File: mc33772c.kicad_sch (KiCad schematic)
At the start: 11 parts, among them U2 MC33772CTP1AE

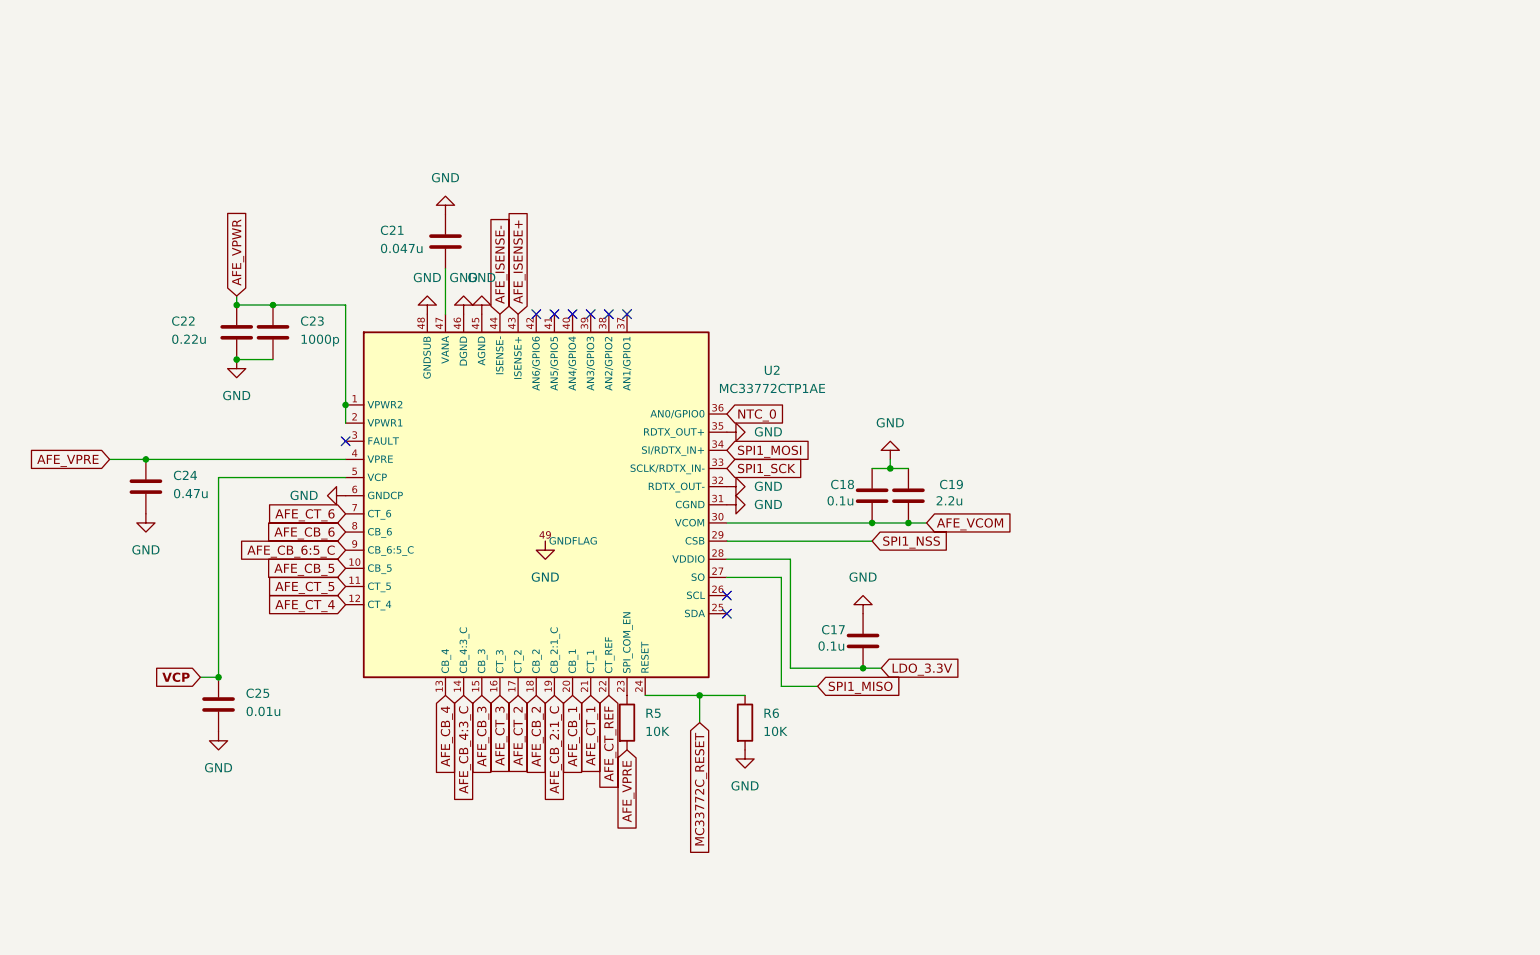
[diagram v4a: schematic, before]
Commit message: add LCPC Part #
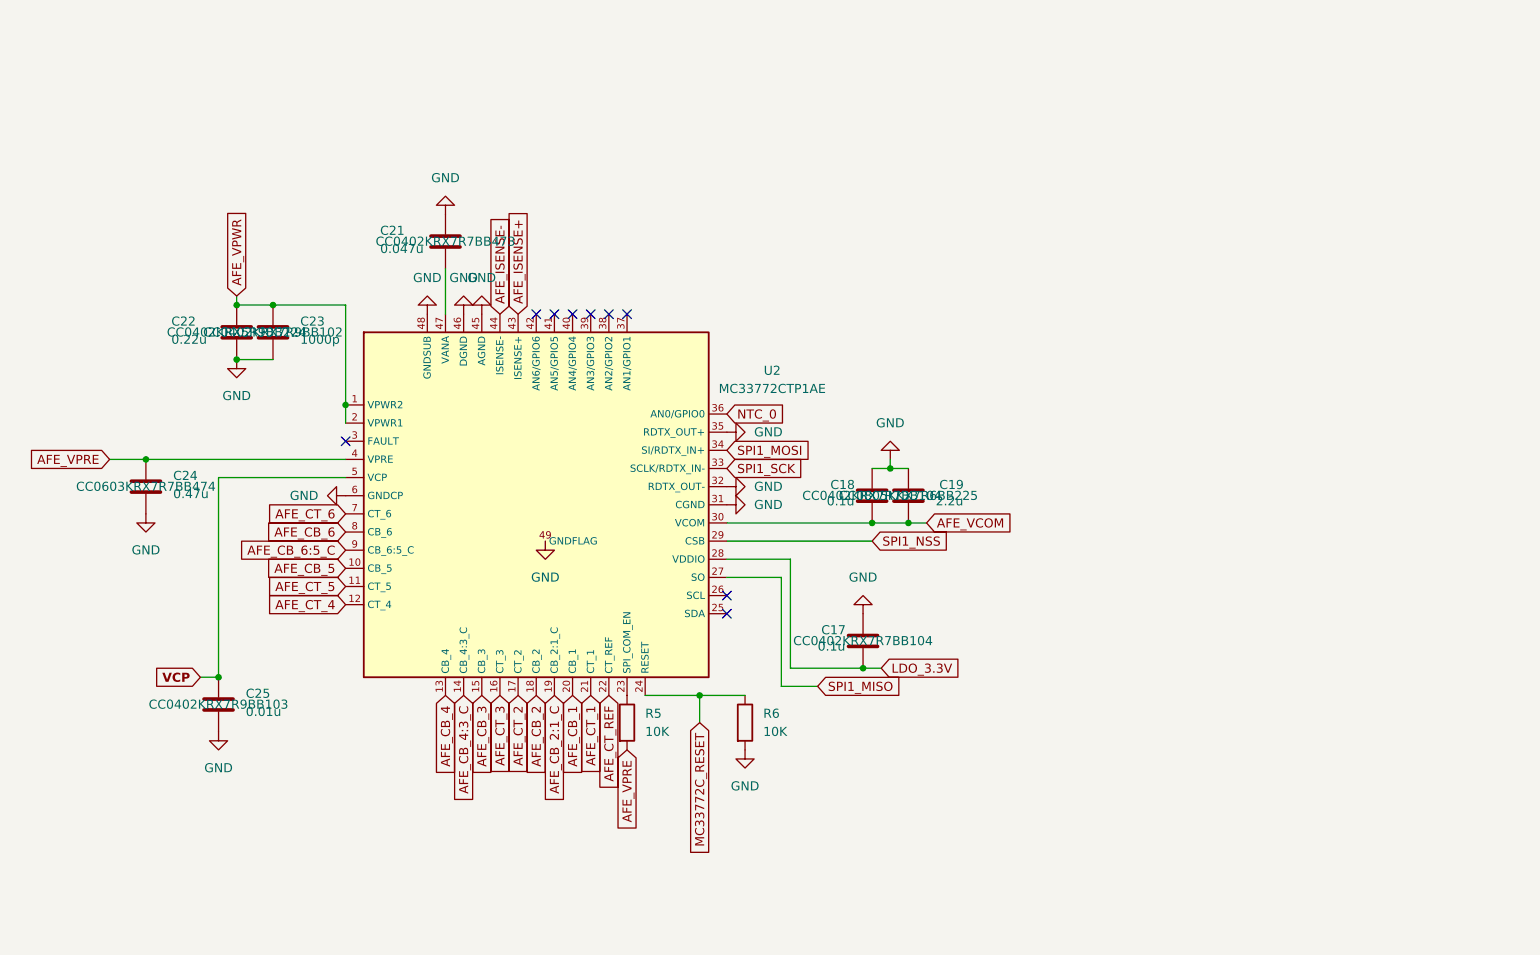
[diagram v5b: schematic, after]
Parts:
- C17, C18: LCSC Part # (none) -> CC0402KRX7R7BB104
- C19: LCSC Part # (none) -> CC0805KKX7R6BB225
- C21: LCSC Part # (none) -> CC0402KRX7R7BB473
- C22: LCSC Part # (none) -> CC0402KRX5R9BB224
- C23: LCSC Part # (none) -> CC0402KRX7R9BB102
- C24: LCSC Part # (none) -> CC0603KRX7R7BB474
- C25: LCSC Part # (none) -> CC0402KRX7R9BB103

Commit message: update for JLCPCB with LCSC part #
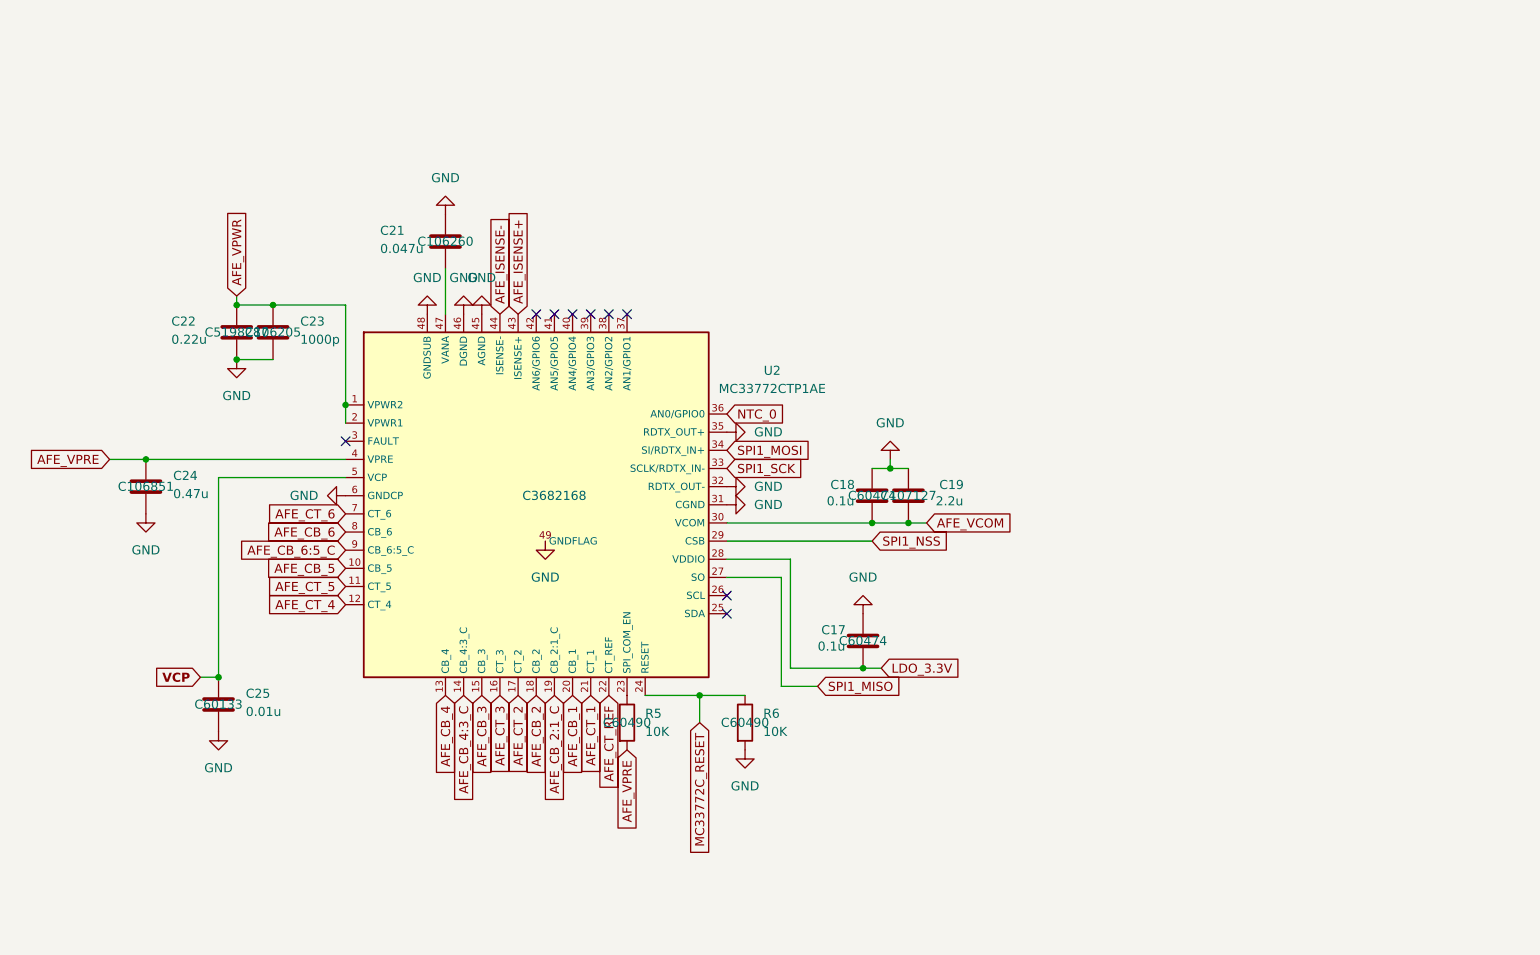
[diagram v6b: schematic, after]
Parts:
- C17, C18: LCSC Part # CC0402KRX7R7BB104 -> C60474
- C19: LCSC Part # CC0805KKX7R6BB225 -> C107127
- C21: LCSC Part # CC0402KRX7R7BB473 -> C106260
- C22: LCSC Part # CC0402KRX5R9BB224 -> C5198287
- C23: LCSC Part # CC0402KRX7R9BB102 -> C106205
- C24: LCSC Part # CC0603KRX7R7BB474 -> C106851
- C25: LCSC Part # CC0402KRX7R9BB103 -> C60133
- R5, R6: LCSC Part # (none) -> C60490
- U2: LCSC Part # (none) -> C3682168
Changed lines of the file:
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@@
 			)
 		)
-		(property "Datasheet" ""
+		(property "Datasheet" "CC0805KKX7R6BB225"
 			(at 200.66 83.82 0)
 			(hide yes)
@@
 			)
 		)
-		(property "LCSC Part #" "CC0805KKX7R6BB225"
+		(property "LCSC Part #" "C107127"
 			(at 200.66 83.82 0)
 			(show_name no)
@@
 			)
 		)
-		(property "Datasheet" ""
+		(property "Datasheet" "CC0603KRX7R7BB474"
 			(at 93.98 82.55 0)
 			(hide yes)
@@
 			)
 		)
-		(property "LCSC Part #" "CC0603KRX7R7BB474"
+		(property "LCSC Part #" "C106851"
 			(at 93.98 82.55 0)
 			(show_name no)
@@
 			)
 		)
-		(property "Datasheet" "https://www.mouser.tw/datasheet/3/508/1/PYu-RC_Group_51_RoHS_L_12.pdf"
+		(property "Datasheet" "RC0402FR-0710KL"
 			(at 177.8 115.57 0)
 			(hide yes)
@@
 			)
 		)
-		(property "Description" "RC0402FR-7D10KL"
+		(property "Description" "RES 10kΩ ±1% 62.5mW 0402"
 			(at 177.8 115.57 0)
 			(hide yes)
@@
 			)
 		)
-		(property "LCSC Part #" ""
+		(property "LCSC Part #" "C60490"
 			(at 177.8 115.57 0)
 			(show_name no)
@@
 			)
 		)
-		(property "Datasheet" ""
+		(property "Datasheet" "CC0402KRX5R9BB224"
 			(at 106.68 60.96 0)
 			(hide yes)
@@
 			)
 		)
-		(property "LCSC Part #" "CC0402KRX5R9BB224"
+		(property "LCSC Part #" "C5198287"
 			(at 106.68 60.96 0)
 			(show_name no)
@@
 			)
 		)
-		(property "Datasheet" ""
+		(property "Datasheet" "CC0402KRX7R9BB103"
 			(at 104.14 113.03 0)
 			(hide yes)
@@
 			)
 		)
-		(property "LCSC Part #" "CC0402KRX7R9BB103"
+		(property "LCSC Part #" "C60133"
 			(at 104.14 113.03 0)
 			(show_name no)
@@
 			)
 		)
-		(property "Description" ""
+		(property "Description" "Battery cell controller IC"
 			(at 146.558 134.62 0)
 			(hide yes)
@@
 			)
 		)
-		(property "LCSC Part #" ""
+		(property "LCSC Part #" "C3682168"
 			(at 151.13 83.82 0)
 			(show_name no)
@@
 			)
 		)
-		(property "Datasheet" ""
+		(property "Datasheet" "CC0402KRX7R7BB104"
 			(at 195.58 83.82 0)
 			(hide yes)
@@
 			)
 		)
-		(property "LCSC Part #" "CC0402KRX7R7BB104"
+		(property "LCSC Part #" "C60474"
 			(at 195.58 83.82 0)
 			(show_name no)
@@
 			)
 		)
-		(property "Datasheet" ""
+		(property "Datasheet" "CC0402KRX7R7BB104"
 			(at 194.31 104.14 0)
 			(hide yes)
@@
 			)
 		)
-		(property "LCSC Part #" "CC0402KRX7R7BB104"
+		(property "LCSC Part #" "C60474"
 			(at 194.31 104.14 0)
 			(show_name no)
@@
 			)
 		)
-		(property "Datasheet" ""
+		(property "Datasheet" "CC0402KRX7R9BB102"
 			(at 111.76 60.96 0)
 			(hide yes)
@@
 			)
 		)
-		(property "LCSC Part #" "CC0402KRX7R9BB102"
+		(property "LCSC Part #" "C106205"
 			(at 111.76 60.96 0)
 			(show_name no)
@@
 			)
 		)
-		(property "Datasheet" ""
+		(property "Datasheet" "RC0402FR-0710KL"
 			(at 161.29 115.57 0)
 			(hide yes)
@@
 			)
 		)
-		(property "Description" "RES MF 10.0K 1/16W 1% AEC-Q200 0402"
+		(property "Description" "RES 10kΩ ±1% 62.5mW 0402"
 			(at 161.29 115.57 0)
 			(hide yes)
@@
 			)
 		)
-		(property "LCSC Part #" ""
+		(property "LCSC Part #" "C60490"
 			(at 161.29 115.57 0)
 			(show_name no)
@@
 			)
 		)
-		(property "Datasheet" ""
+		(property "Datasheet" "CC0402KRX7R7BB473"
 			(at 135.89 48.26 0)
 			(hide yes)
@@
 			)
 		)
-		(property "LCSC Part #" "CC0402KRX7R7BB473"
+		(property "LCSC Part #" "C106260"
 			(at 135.89 48.26 0)
 			(show_name no)

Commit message: export to JLCPCB
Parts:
- C17, C18: value 0.1u -> 100n
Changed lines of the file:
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@@
 			)
 		)
-		(property "Value" "0.1u"
+		(property "Value" "100n"
 			(at 189.23 84.582 0)
 			(show_name no)
@@
 			)
 		)
-		(property "Value" "0.1u"
+		(property "Value" "100n"
 			(at 187.96 104.902 0)
 			(show_name no)

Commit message: for PCBWay
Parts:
- C17, C18: MPN (none) -> CC0402KRX7R7BB104
- C19: MPN (none) -> CC0805KKX7R6BB225
- C21: MPN (none) -> CC0402KRX7R7BB473
- C22: MPN (none) -> CC0402KRX5R9BB224
- C23: MPN (none) -> CC0402KRX7R9BB102
- C24: MPN (none) -> CC0603KRX7R7BB474
- C25: MPN (none) -> CC0402KRX7R9BB103
- R5, R6: MPN (none) -> RC0402FR-0710KL
- U2: MPN (none) -> MC33772CTP1AE
